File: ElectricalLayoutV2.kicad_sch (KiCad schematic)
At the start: 34 parts, among them K1 3.3V-24V (40A), K2 Relay_SPST-NO, K3 Relay_SPST-NO, K4 Relay_SPST-NO, SW1 SW_Push, SW3 SW_Push

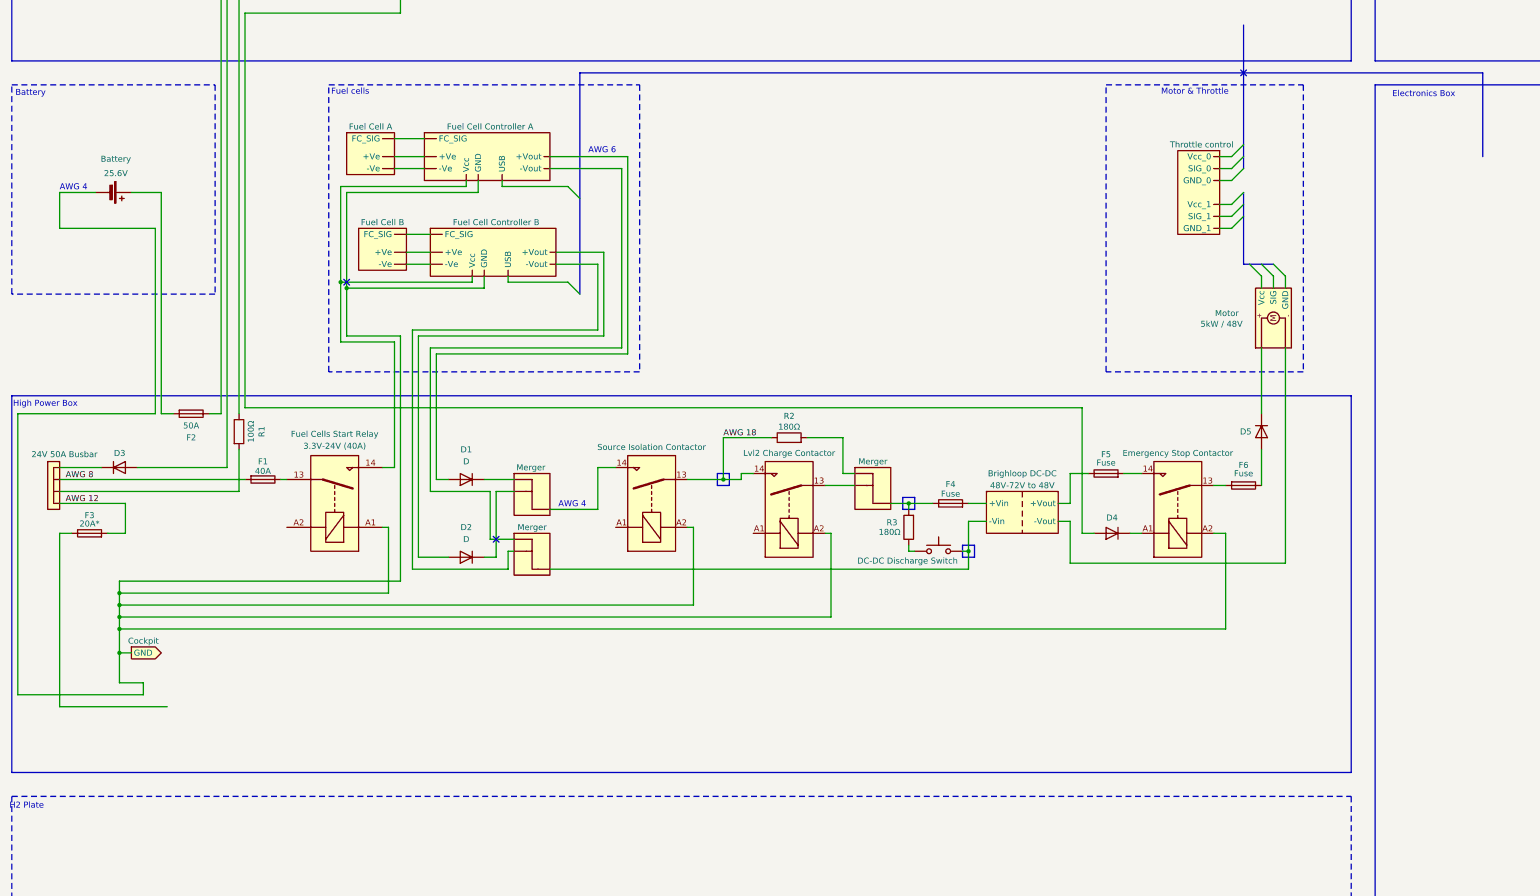
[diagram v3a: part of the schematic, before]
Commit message: Zone coloring and label placement
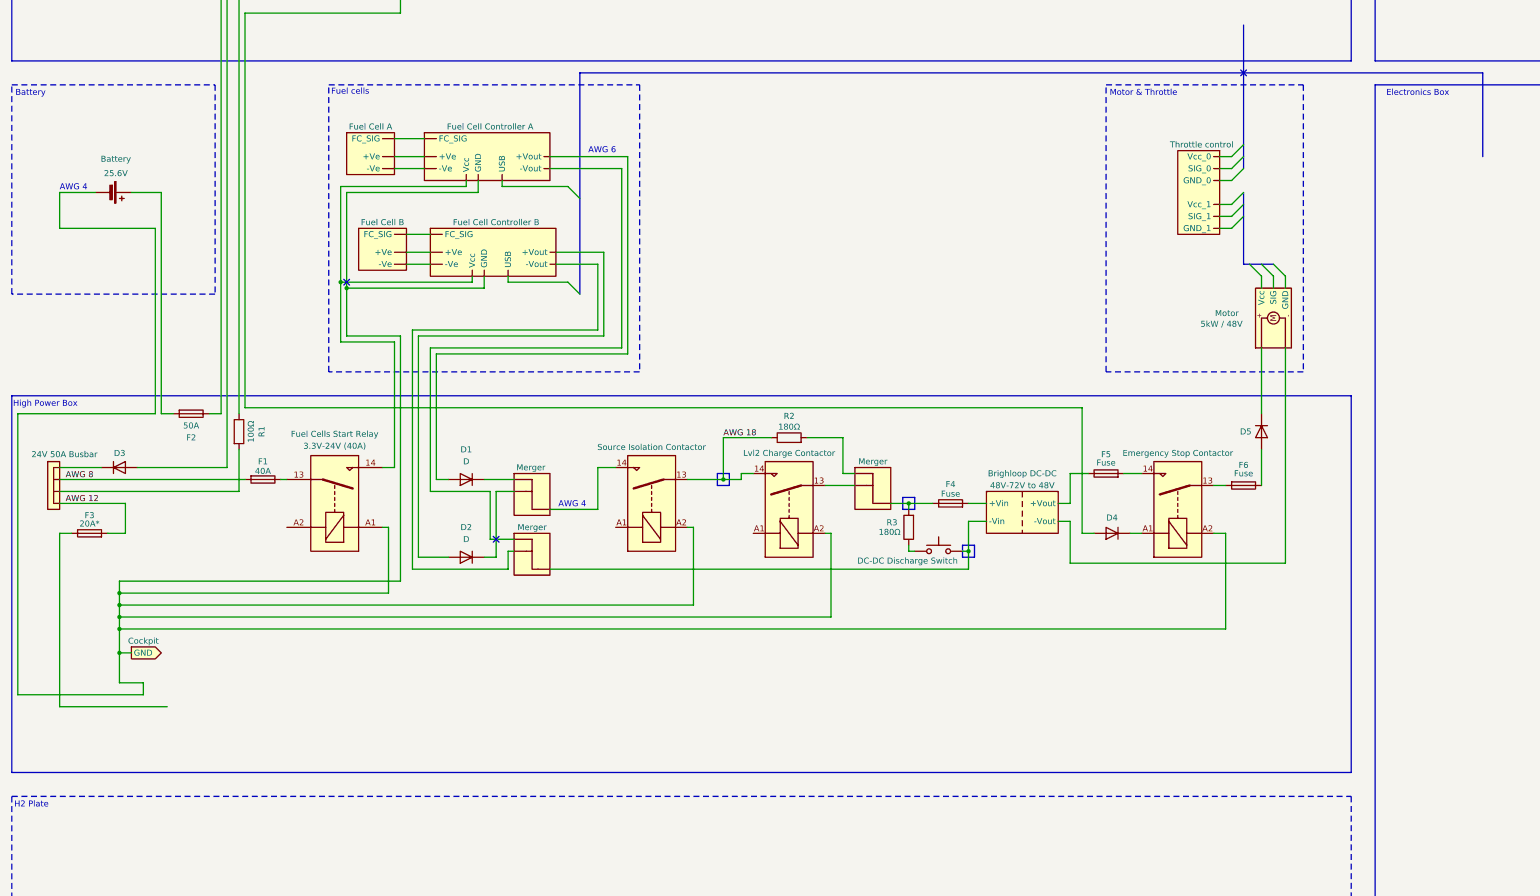
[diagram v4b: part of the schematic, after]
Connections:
- net at FCC2. (Vcc): now also MRG2.; no longer FC3. (FC_SIG)
- net at DCC1. (-Vout): now also F5.1; no longer PROP1. (Vcc)
- net at MRG2.: now also FCC1. (Vcc); no longer FCC2. (Vcc)
- new net: FC3. (FC_SIG), FCC2. (Vcc) (x2)
- new net: DCC1. (-Vout), PROP1. (Vcc)
- new net: DCC1. (-Vout), MRG2., SW3.2
- new net: FCC1. (Vcc), FCC2. (Vcc), K1.14
- new net: FC4. (FC_SIG), FCC1. (Vcc) (x2)
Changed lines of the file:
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@@
 			(width 0)
 			(type default)
+			(color 132 0 132 1)
 		)
 		(fill
@@
 	(text "H2 Plate"
 		(exclude_from_sim no)
-		(at 13.462 217.424 0)
+		(at 14.478 217.17 0)
 		(effects
 			(font
@@
 	(text "Motor & Throttle"
 		(exclude_from_sim no)
-		(at 258.064 65.786 0)
+		(at 247.142 66.04 0)
 		(effects
 			(font
@@
 	(text "Electronics Box"
 		(exclude_from_sim no)
-		(at 320.548 66.294 0)
+		(at 319.278 66.04 0)
 		(effects
 			(font

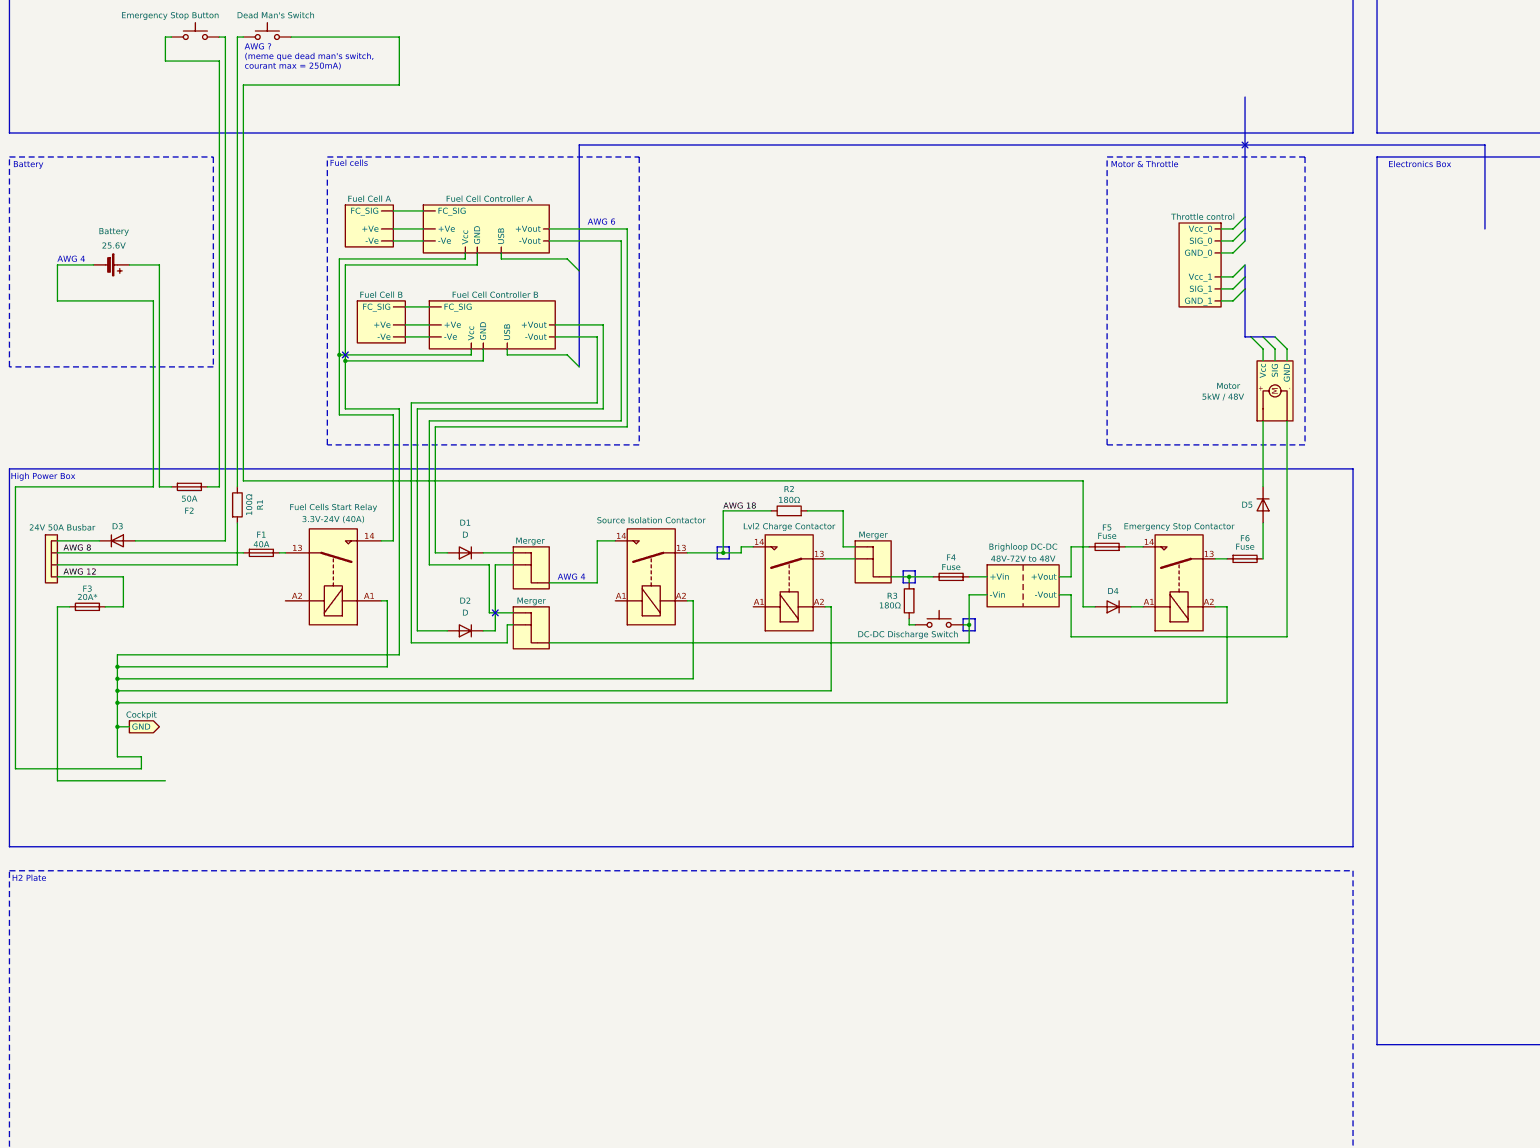
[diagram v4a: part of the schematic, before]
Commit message: H2 Plate, Precharge and DC-DC update
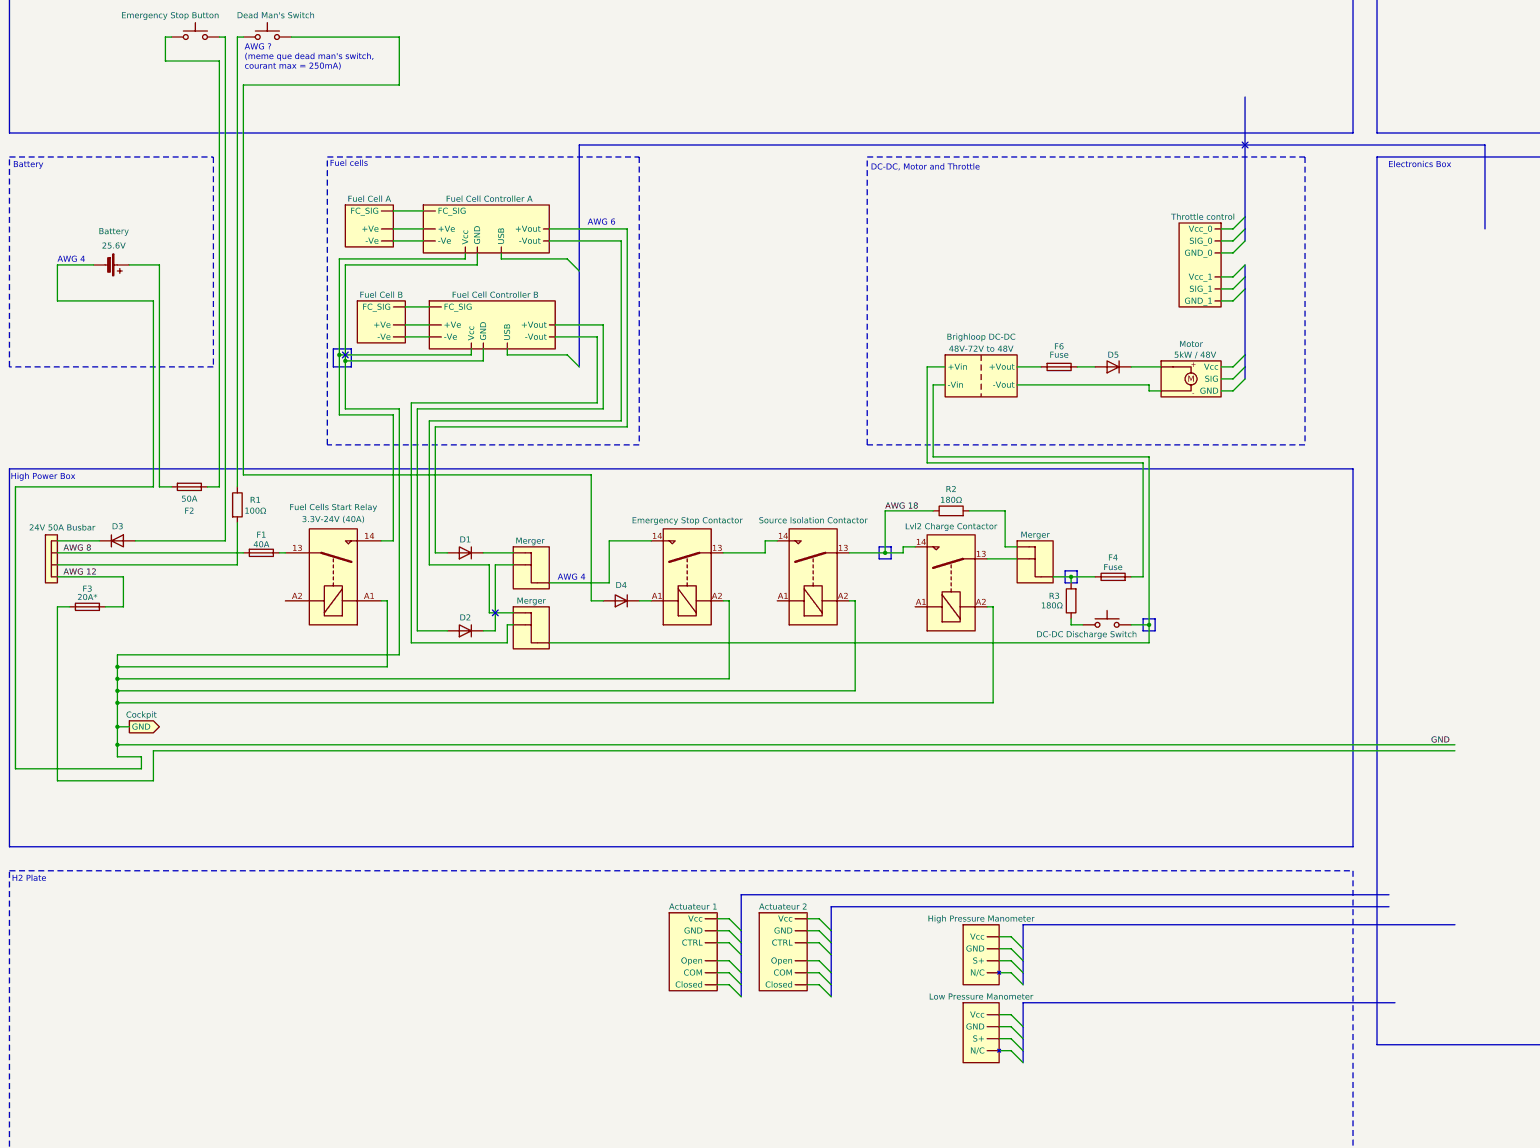
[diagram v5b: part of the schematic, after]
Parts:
- removed F5: Fuse, symbol Device:Fuse
- added ACT1, ACT2: ~, symbol Exocet_Electrical:Valve_Actuator
- added MAN1, MAN2: ~, symbol Exocet_Electrical:Manometer
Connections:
- net at K2.13: now also K3.14; no longer F6.2
- net at K2.14: now also MRG1.
- net GND: now reaches B2.2 (-), CGND1. (GND), FCC1. (Vcc), FCC2. (Vcc), K1.A1, K2.A2, K3.A2, K4.A2
- net at DCC1. (-Vout): now also F6.2; no longer PROP1. (Vcc)
- net at MRG1.: now also D1.1 (K); no longer K3.14
- net at MRG2.: now also FCC1. (Vcc); no longer FCC2. (Vcc)
- new net: FC3. (FC_SIG), FCC2. (Vcc) (x2)
- new net: DCC1. (-Vout), PROP1. (Vcc)
- new net: DCC1. (-Vout), MRG2., SW3.2
- new net: FCC1. (Vcc), FCC2. (Vcc), K1.14
- new net: FCC2. (Vcc), MRG2.
- new net: FC4. (FC_SIG), FCC1. (Vcc) (x2)
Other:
- note added: "DC-DC, Motor and Throttle"
- note removed: "Motor & Throttle"
- moved on the sheet: D4, F4, R2, R3

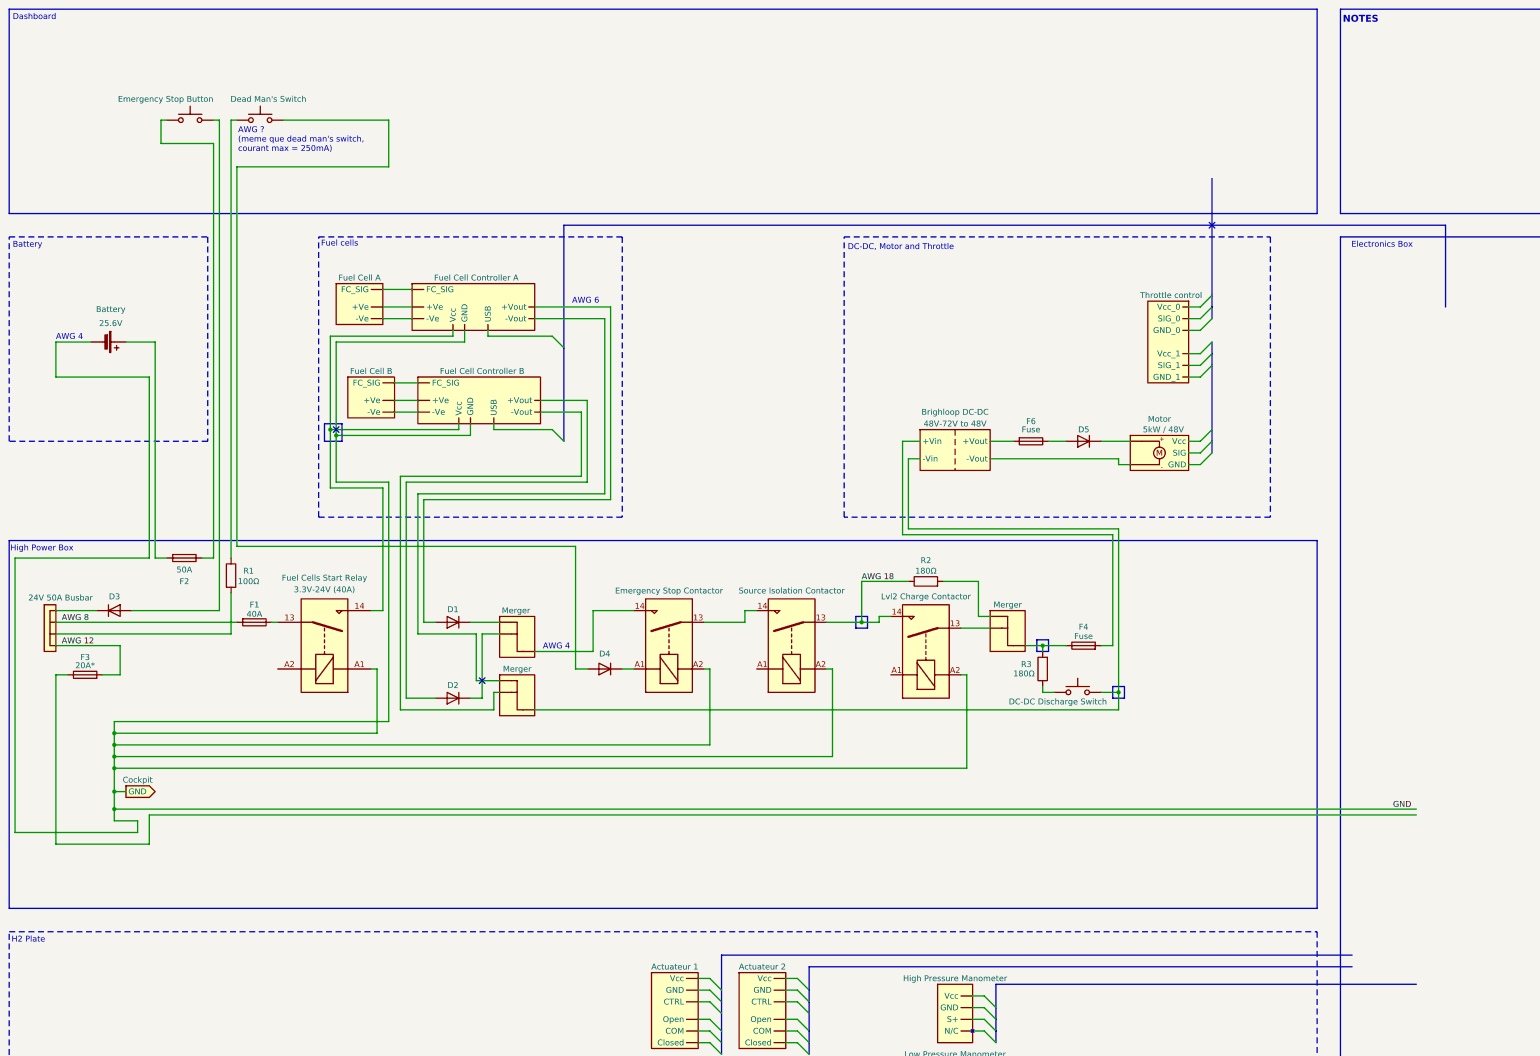
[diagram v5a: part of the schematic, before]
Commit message: Dashboard and temperature sensors
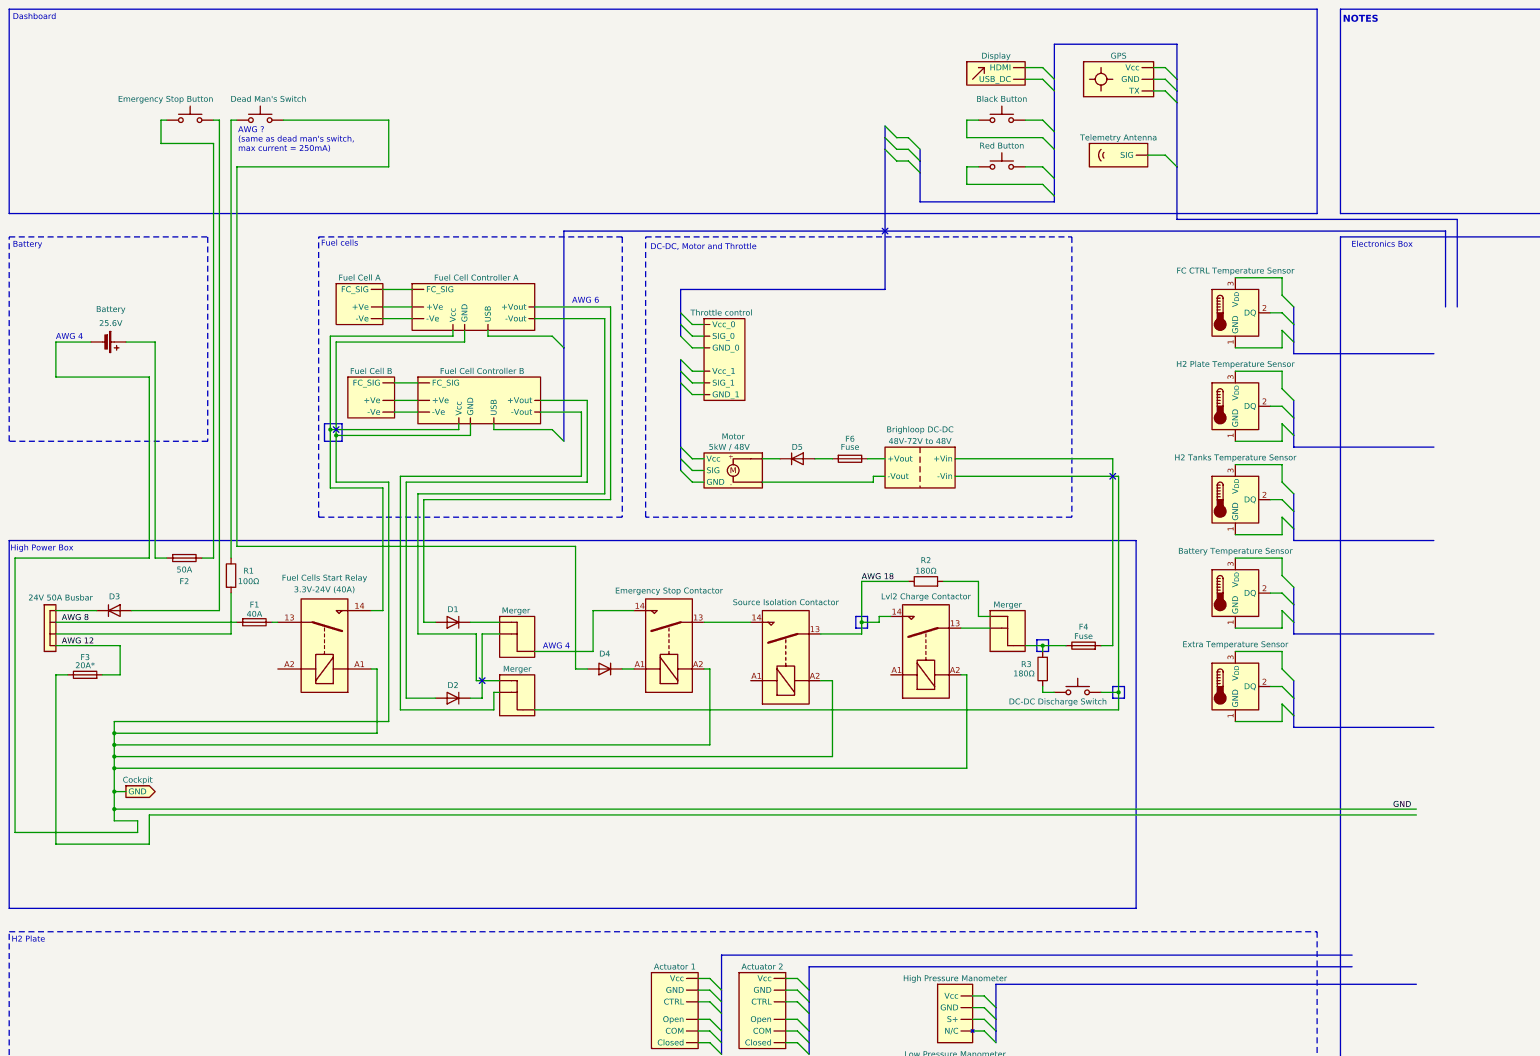
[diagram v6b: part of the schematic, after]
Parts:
- added ANT1: ~, symbol Exocet_Electrical:Antenna
- added DSP1: ~, symbol Exocet_Electrical:Display
- added GPS1: ~, symbol Exocet_Electrical:GPS
- added SW4, SW5: SW_Push, symbol Switch:SW_Push
- added U1, U2, U3, U4, U5: DS18B20, Package_TO_SOT_THT:TO-92_Inline, symbol Sensor_Temperature:DS18B20
- ACT1: Name Actuateur 1 -> Actuator 1
- ACT2: Name Actuateur 2 -> Actuator 2
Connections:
- net at DCC1. (-Vout): now also F6.1; no longer PROP1. (Vcc)
- net at F6.2: now also D5.2 (A); no longer DCC1. (-Vout)
- net at MRG2.: now also FCC1. (Vcc); no longer FCC2. (Vcc)
- new net: FC3. (FC_SIG), FCC2. (Vcc) (x2)
- new net: DCC1. (-Vout), PROP1. (Vcc)
- new net: DCC1. (-Vout), MRG2., SW3.2
- new net: FCC1. (Vcc), FCC2. (Vcc), K1.14
- new net: FCC2. (Vcc), MRG2.
- new net: FC4. (FC_SIG), FCC1. (Vcc) (x2)
- no-connect marks 3 -> 4
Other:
- note added: "AWG ? (same as dead man's switch, max current = 250mA)"
- note removed: "AWG ? (meme que dead man's switch, courant max = 250mA)"
- moved on the sheet: F6
